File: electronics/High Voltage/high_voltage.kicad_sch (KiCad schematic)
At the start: 190 parts, among them J1 EG HV, J2 FILAMENT, J3 BIAS, J4 Conn_01x07_Socket, J5 Conn_01x03_Pin, Q1 Q_NPN, Q4 Q_NPN, Q6 Q_NPN, Y1 DC 24V, Y2 DC 24V

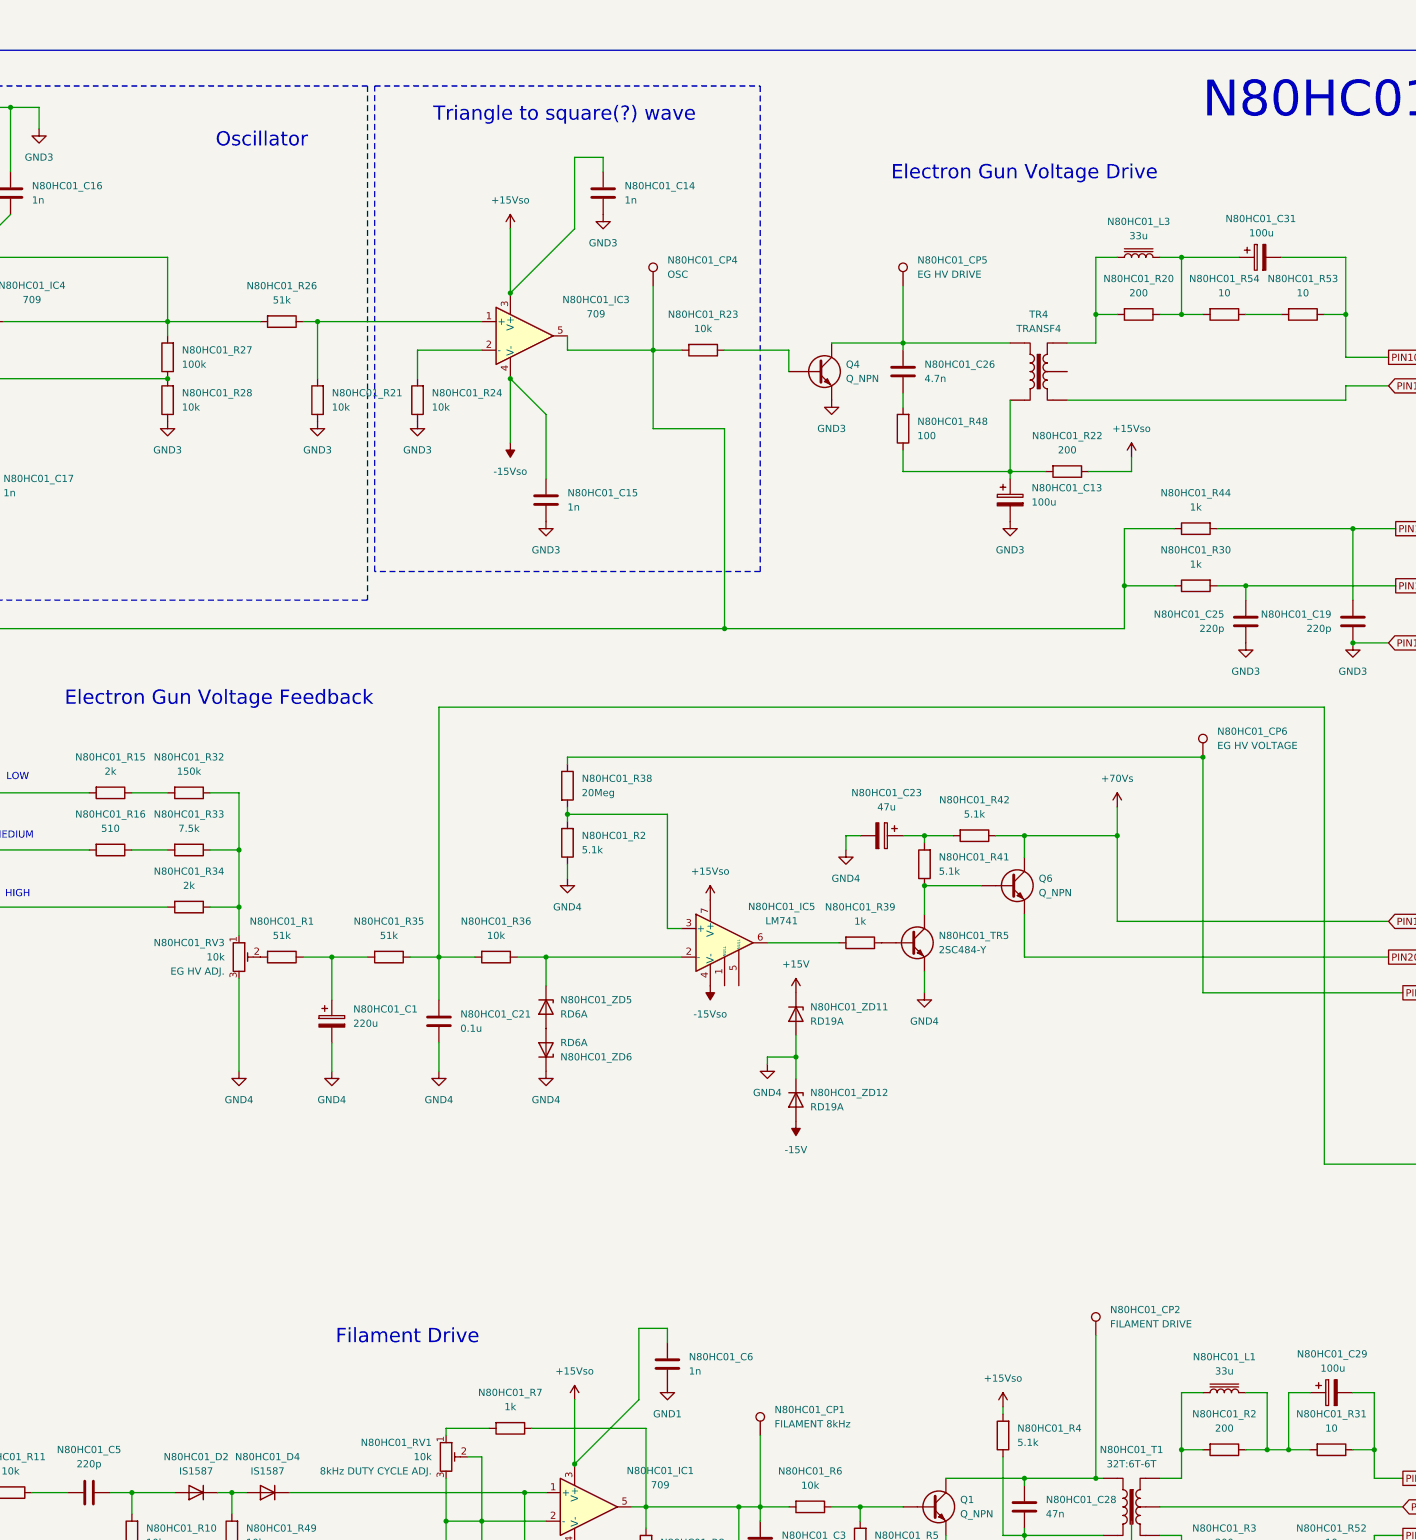
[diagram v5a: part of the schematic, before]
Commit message: Corrections to HV driver operation
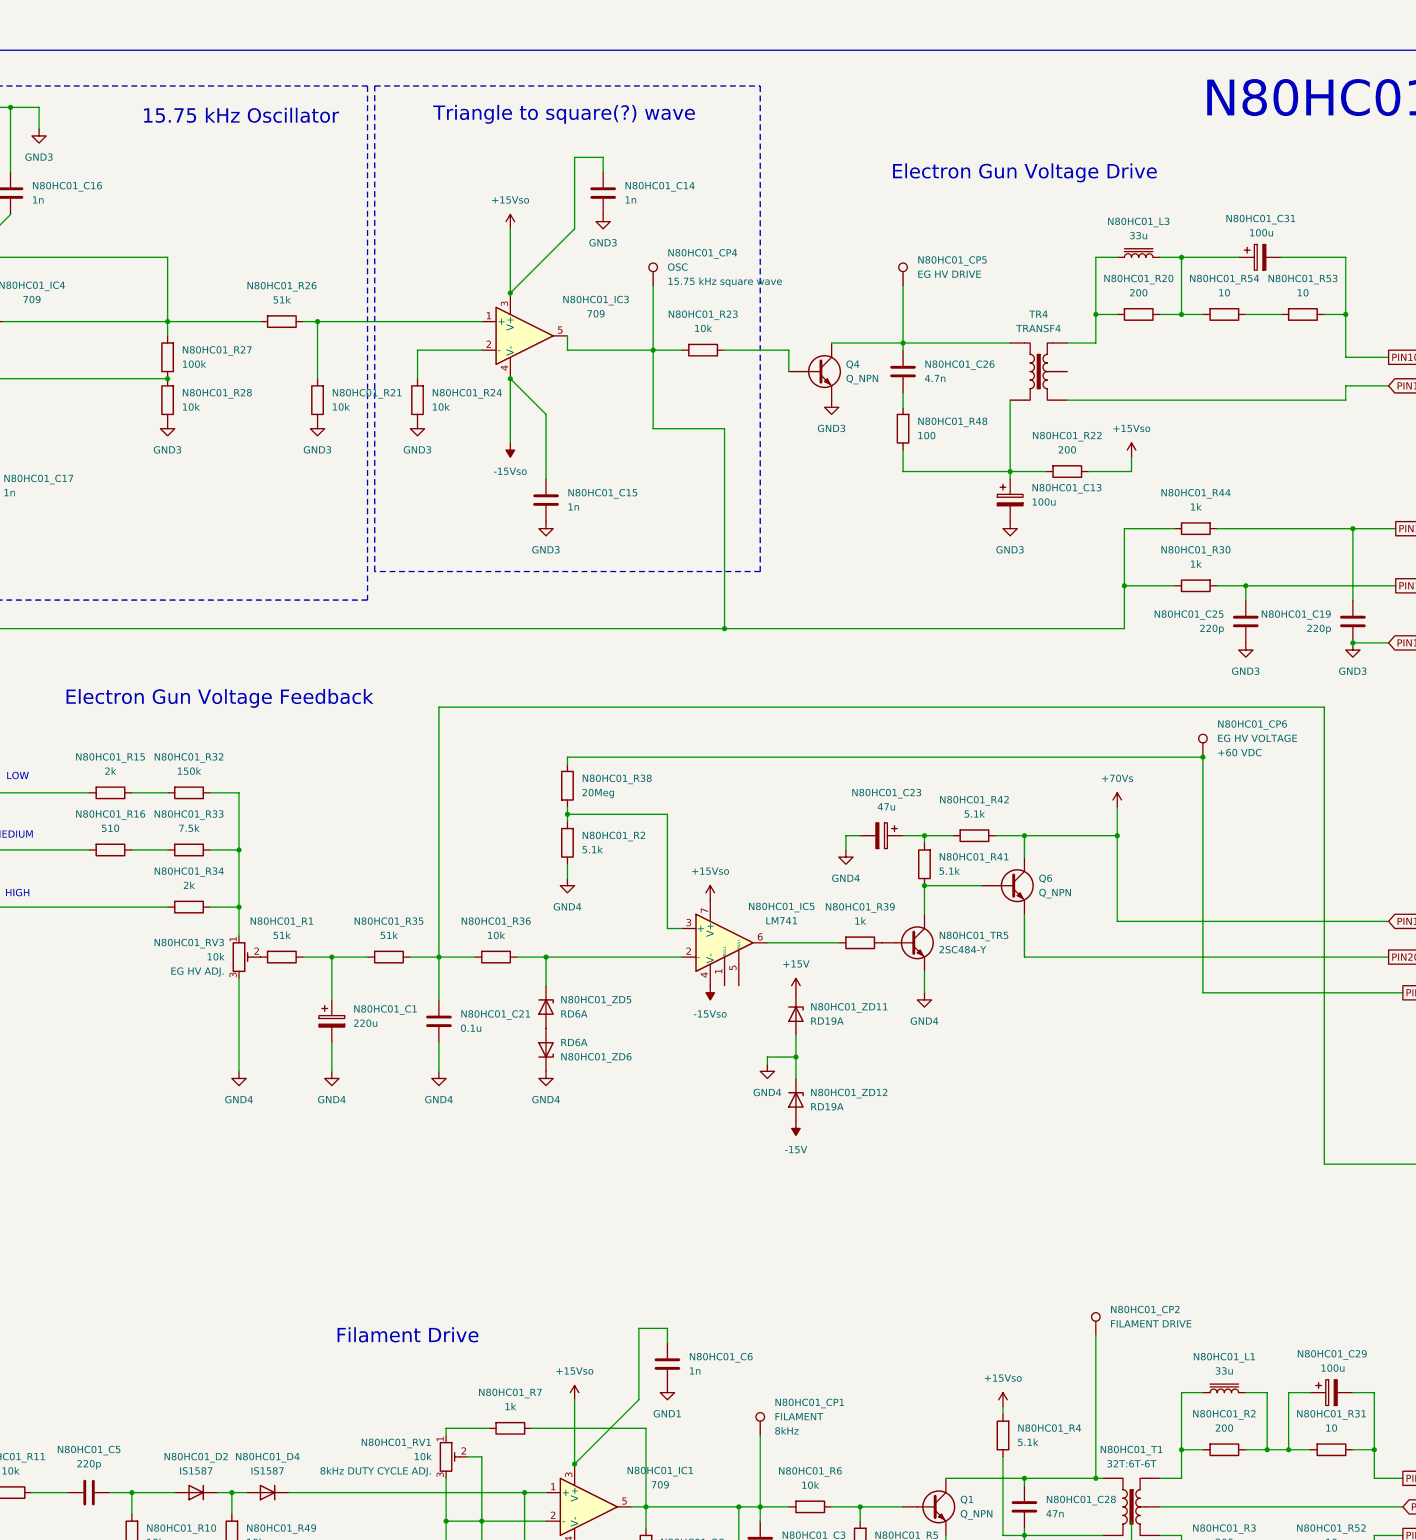
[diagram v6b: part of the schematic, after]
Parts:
- N80HC01_CP1: value FILAMENT 8kHz -> FILAMENT
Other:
- note added: "15.75 kHz Oscillator"
- note removed: "Oscillator"
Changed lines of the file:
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@@
 		)
 	)
-	(text "Oscillator"
+	(text "15.75 kHz Oscillator"
 		(exclude_from_sim no)
-		(at 192.024 42.672 0)
+		(at 188.214 38.608 0)
 		(effects
 			(font
@@
 		(fields_autoplaced yes)
 		(property "Reference" "N80HC01_CP6"
-			(at 361.95 147.8279 0)
+			(at 361.95 146.5579 0)
 			(effects
 				(font
@@
 		)
 		(property "Value" "EG HV VOLTAGE"
-			(at 361.95 150.3679 0)
+			(at 361.95 149.0979 0)
 			(effects
 				(font
@@
 			)
 		)
-		(property "Description" "test point"
-			(at 359.41 152.4 0)
+		(property "Description" "+60 VDC"
+			(at 361.95 151.6379 0)
 			(effects
 				(font
 					(size 1.27 1.27)
 				)
-				(hide yes)
+				(justify left)
 			)
 		)
@@
 		(fields_autoplaced yes)
 		(property "Reference" "N80HC01_CP1"
-			(at 283.21 268.4779 0)
+			(at 283.21 267.2079 0)
 			(effects
 				(font
@@
 			)
 		)
-		(property "Value" "FILAMENT 8kHz"
-			(at 283.21 271.0179 0)
+		(property "Value" "FILAMENT"
+			(at 283.21 269.7479 0)
 			(effects
 				(font
@@
 			)
 		)
-		(property "Description" "test point"
-			(at 280.67 273.05 0)
+		(property "Description" "8kHz"
+			(at 283.21 272.2879 0)
 			(effects
 				(font
 					(size 1.27 1.27)
 				)
-				(hide yes)
+				(justify left)
 			)
 		)
@@
 		(fields_autoplaced yes)
 		(property "Reference" "N80HC01_CP4"
-			(at 264.16 64.0079 0)
+			(at 264.16 62.7379 0)
 			(effects
 				(font
@@
 		)
 		(property "Value" "OSC"
-			(at 264.16 66.5479 0)
+			(at 264.16 65.2779 0)
 			(effects
 				(font
@@
 			)
 		)
-		(property "Description" "test point"
-			(at 261.62 68.58 0)
+		(property "Description" "15.75 kHz square wave"
+			(at 264.16 67.8179 0)
 			(effects
 				(font
 					(size 1.27 1.27)
 				)
-				(hide yes)
+				(justify left)
 			)
 		)
@@
 			)
 		)
-		(property "Description" "test point"
-			(at 306.07 68.58 0)
+		(property "Description" ""
+			(at 308.61 67.8179 0)
 			(effects
 				(font
 					(size 1.27 1.27)
 				)
+				(justify left)
 				(hide yes)
 			)
